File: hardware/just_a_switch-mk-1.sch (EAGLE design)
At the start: 9 parts, among them Q1 2N7000

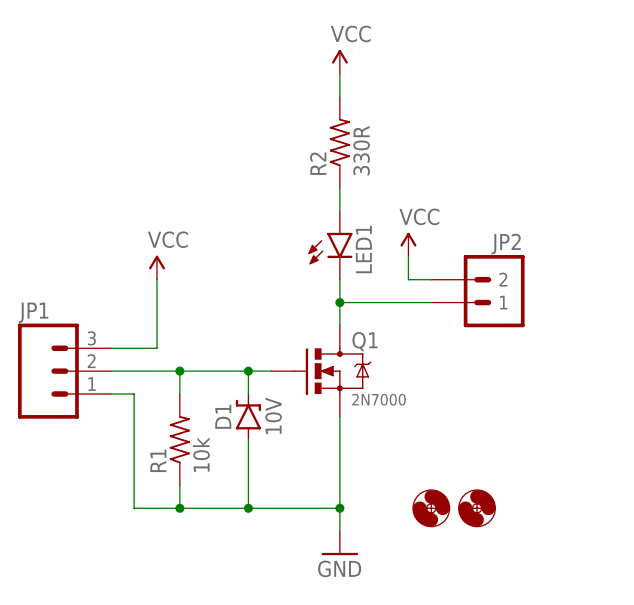
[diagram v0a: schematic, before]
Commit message: Stupid simple N-MOSFET breakout with LED for debugging
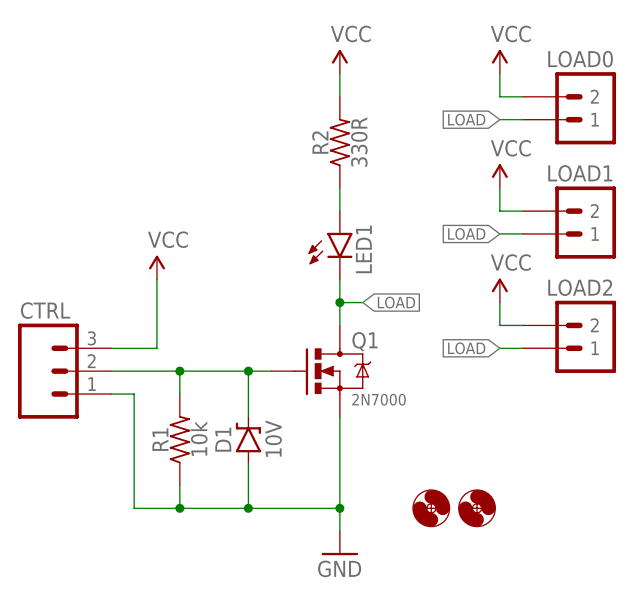
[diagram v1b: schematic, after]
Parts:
- removed JP2: M02PTH, A_butts:M02PTH
- added LOAD0: M02PTH-2MM, A_butts:M02PTH-2MM
- added LOAD1: M021X02_NO_SILK, A_butts:M021X02_NO_SILK
- added LOAD2: M023.5MM, A_butts:M023.5MM
- D1: device A_butts:DIODE-ZENERPTH-7.68MM -> A_butts:DIODE-ZENERPTH-7.62MM
- R1, R2: device A_butts:RESISTORPTH-AXIAL-5.08MM -> A_butts:RESISTORPTH-AXIAL-7.62MM
- renumbered JP1 to CTRL
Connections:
- removed net N$3: JP2.1, LED1.C, Q1.D
- new net LOAD: LED1.C, LOAD0.1, LOAD1.1, LOAD2.1, Q1.D
- net VCC: now also LOAD0.2, LOAD1.2, LOAD2.2; no longer JP2.2
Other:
- moved on the sheet: D1
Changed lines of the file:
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@@
 <parts>
 <part name="Q1" library="A_butts" deviceset="MOSFET-NCHANNEL" device="2N7000-AMMO" value="2N7000"/>
-<part name="R1" library="A_butts" deviceset="RESISTOR" device="PTH-AXIAL-5.08MM" value="10k"/>
-<part name="R2" library="A_butts" deviceset="RESISTOR" device="PTH-AXIAL-5.08MM" value="330R"/>
-<part name="D1" library="A_butts" deviceset="DIODE-ZENER" device="PTH-7.68MM" value="10V"/>
+<part name="R1" library="A_butts" deviceset="RESISTOR" device="PTH-AXIAL-7.62MM" value="10k"/>
+<part name="R2" library="A_butts" deviceset="RESISTOR" device="PTH-AXIAL-7.62MM" value="330R"/>
+<part name="D1" library="A_butts" deviceset="DIODE-ZENER" device="PTH-7.62MM" value="10V"/>
 <part name="GND1" library="A_butts" deviceset="GND" device=""/>
 <part name="H1" library="A_butts" deviceset="HOLE" device="#2"/>
@@
 <part name="SUPPLY1" library="A_butts" deviceset="VCC" device=""/>
 <part name="SUPPLY3" library="A_butts" deviceset="VCC" device=""/>
-<part name="JP1" library="A_butts" deviceset="M03" device="PTH"/>
-<part name="JP2" library="A_butts" deviceset="M02" device="PTH"/>
+<part name="CTRL" library="A_butts" deviceset="M03" device="PTH"/>
+<part name="LOAD0" library="A_butts" deviceset="M02" device="PTH-2MM" value="M02PTH-2MM"/>
 <part name="SUPPLY2" library="A_butts" deviceset="VCC" device=""/>
+<part name="LOAD1" library="A_butts" deviceset="M02" device="1X02_NO_SILK" value="M021X02_NO_SILK"/>
+<part name="LOAD2" library="A_butts" deviceset="M02" device="3.5MM" value="M023.5MM"/>
+<part name="SUPPLY4" library="A_butts" deviceset="VCC" device=""/>
+<part name="SUPPLY5" library="A_butts" deviceset="VCC" device=""/>
 </parts>
 <sheets>
@@
 <instance part="R1" gate="G$1" x="63.5" y="43.18" rot="R90"/>
 <instance part="R2" gate="G$1" x="81.28" y="76.2" rot="R90"/>
-<instance part="D1" gate="G$1" x="71.12" y="45.72" rot="R90"/>
+<instance part="D1" gate="G$1" x="71.12" y="43.18" rot="R90"/>
 <instance part="GND1" gate="1" x="81.28" y="30.48"/>
 <instance part="H1" gate="G$1" x="91.44" y="35.56"/>
@@
 <instance part="SUPPLY1" gate="G$1" x="60.96" y="60.96"/>
 <instance part="SUPPLY3" gate="G$1" x="81.28" y="83.82"/>
-<instance part="JP1" gate="G$1" x="48.26" y="50.8"/>
-<instance part="JP2" gate="G$1" x="101.6" y="55.88" rot="MR0"/>
-<instance part="SUPPLY2" gate="G$1" x="88.9" y="63.5"/>
+<instance part="CTRL" gate="G$1" x="48.26" y="50.8"/>
+<instance part="LOAD0" gate="G$1" x="111.76" y="76.2" rot="MR0"/>
+<instance part="SUPPLY2" gate="G$1" x="99.06" y="83.82"/>
+<instance part="LOAD1" gate="G$1" x="111.76" y="63.5" rot="MR0"/>
+<instance part="LOAD2" gate="G$1" x="111.76" y="50.8" rot="MR0"/>
+<instance part="SUPPLY4" gate="G$1" x="99.06" y="71.12"/>
+<instance part="SUPPLY5" gate="G$1" x="99.06" y="58.42"/>
 </instances>
 <busses>
@@
 <segment>
 <pinref part="D1" gate="G$1" pin="C"/>
-<wire x1="71.12" y1="50.8" x2="71.12" y2="48.26" width="0.1524" layer="91"/>
+<wire x1="71.12" y1="50.8" x2="71.12" y2="45.72" width="0.1524" layer="91"/>
 <pinref part="Q1" gate="G$1" pin="G"/>
 <wire x1="71.12" y1="50.8" x2="73.66" y2="50.8" width="0.1524" layer="91"/>
@@
 <wire x1="55.88" y1="50.8" x2="63.5" y2="50.8" width="0.1524" layer="91"/>
 <junction x="63.5" y="50.8"/>
-<pinref part="JP1" gate="G$1" pin="2"/>
+<pinref part="CTRL" gate="G$1" pin="2"/>
 </segment>
 </net>
@@
 <segment>
 <pinref part="D1" gate="G$1" pin="A"/>
-<wire x1="71.12" y1="43.18" x2="71.12" y2="35.56" width="0.1524" layer="91"/>
+<wire x1="71.12" y1="40.64" x2="71.12" y2="35.56" width="0.1524" layer="91"/>
 <wire x1="71.12" y1="35.56" x2="81.28" y2="35.56" width="0.1524" layer="91"/>
 <pinref part="GND1" gate="1" pin="GND"/>
@@
 <wire x1="58.42" y1="35.56" x2="63.5" y2="35.56" width="0.1524" layer="91"/>
 <junction x="63.5" y="35.56"/>
-<pinref part="JP1" gate="G$1" pin="1"/>
+<pinref part="CTRL" gate="G$1" pin="1"/>
 </segment>
 </net>
@@
 </segment>
 </net>
-<net name="N$3" class="0">
+<net name="LOAD" class="0">
 <segment>
 <pinref part="LED1" gate="G$1" pin="C"/>
 <pinref part="Q1" gate="G$1" pin="D"/>
 <wire x1="81.28" y1="55.88" x2="81.28" y2="58.42" width="0.1524" layer="91"/>
-<pinref part="JP2" gate="G$1" pin="1"/>
 <wire x1="81.28" y1="58.42" x2="81.28" y2="60.96" width="0.1524" layer="91"/>
-<wire x1="81.28" y1="58.42" x2="91.44" y2="58.42" width="0.1524" layer="91"/>
+<wire x1="81.28" y1="58.42" x2="83.82" y2="58.42" width="0.1524" layer="91"/>
 <junction x="81.28" y="58.42"/>
+<label x="83.82" y="58.42" size="1.27" layer="95" xref="yes"/>
+</segment>
+<segment>
+<pinref part="LOAD0" gate="G$1" pin="1"/>
+<wire x1="99.06" y1="78.74" x2="101.6" y2="78.74" width="0.1524" layer="91"/>
+<label x="99.06" y="78.74" size="1.27" layer="95" rot="R180" xref="yes"/>
+</segment>
+<segment>
+<pinref part="LOAD1" gate="G$1" pin="1"/>
+<wire x1="99.06" y1="66.04" x2="101.6" y2="66.04" width="0.1524" layer="91"/>
+<label x="99.06" y="66.04" size="1.27" layer="95" rot="R180" xref="yes"/>
+</segment>
+<segment>
+<pinref part="LOAD2" gate="G$1" pin="1"/>
+<wire x1="99.06" y1="53.34" x2="101.6" y2="53.34" width="0.1524" layer="91"/>
+<label x="99.06" y="53.34" size="1.27" layer="95" rot="R180" xref="yes"/>
 </segment>
 </net>
@@
 <wire x1="60.96" y1="53.34" x2="60.96" y2="60.96" width="0.1524" layer="91"/>
 <pinref part="SUPPLY1" gate="G$1" pin="VCC"/>
-<pinref part="JP1" gate="G$1" pin="3"/>
+<pinref part="CTRL" gate="G$1" pin="3"/>
 </segment>
 <segment>
 <pinref part="SUPPLY2" gate="G$1" pin="VCC"/>
-<wire x1="88.9" y1="63.5" x2="88.9" y2="60.96" width="0.1524" layer="91"/>
-<pinref part="JP2" gate="G$1" pin="2"/>
-<wire x1="88.9" y1="60.96" x2="91.44" y2="60.96" width="0.1524" layer="91"/>
+<wire x1="99.06" y1="83.82" x2="99.06" y2="81.28" width="0.1524" layer="91"/>
+<pinref part="LOAD0" gate="G$1" pin="2"/>
+<wire x1="99.06" y1="81.28" x2="101.6" y2="81.28" width="0.1524" layer="91"/>
+</segment>
+<segment>
+<pinref part="SUPPLY5" gate="G$1" pin="VCC"/>
+<wire x1="99.06" y1="58.42" x2="99.06" y2="55.88" width="0.1524" layer="91"/>
+<pinref part="LOAD2" gate="G$1" pin="2"/>
+<wire x1="99.06" y1="55.88" x2="101.6" y2="55.88" width="0.1524" layer="91"/>
+</segment>
+<segment>
+<pinref part="SUPPLY4" gate="G$1" pin="VCC"/>
+<wire x1="99.06" y1="71.12" x2="99.06" y2="68.58" width="0.1524" layer="91"/>
+<pinref part="LOAD1" gate="G$1" pin="2"/>
+<wire x1="99.06" y1="68.58" x2="101.6" y2="68.58" width="0.1524" layer="91"/>
 </segment>
 </net>
